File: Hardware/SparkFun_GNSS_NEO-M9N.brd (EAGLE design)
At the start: 64.9 x 38 mm, 74 parts, among them J1 MICROMOD_STANDARD, J4 Bus Selection, U1 U-BLOX_NEO-M9N, U2 3.3V, U3 EEPROM, U4 74HC1G04

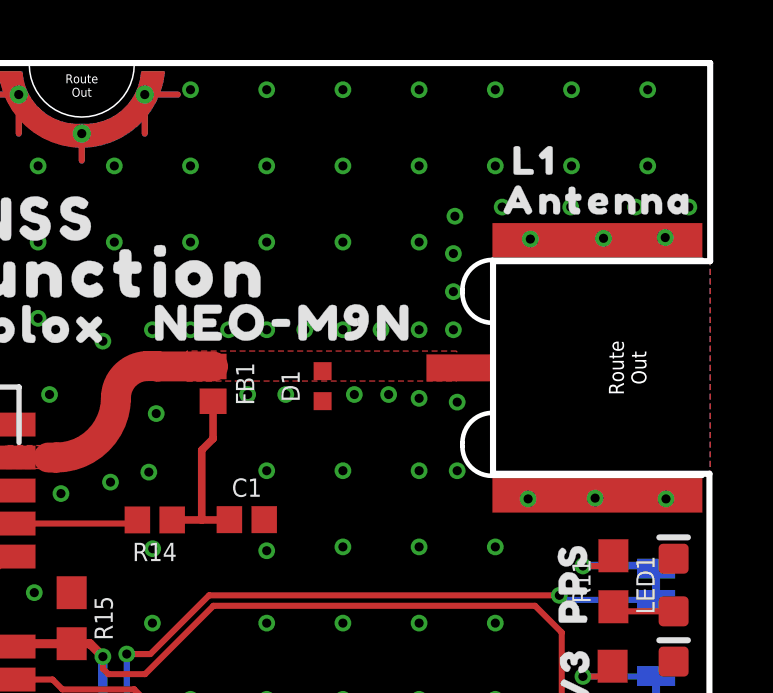
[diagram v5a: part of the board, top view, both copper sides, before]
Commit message: Switches SMA connector to PTH connector
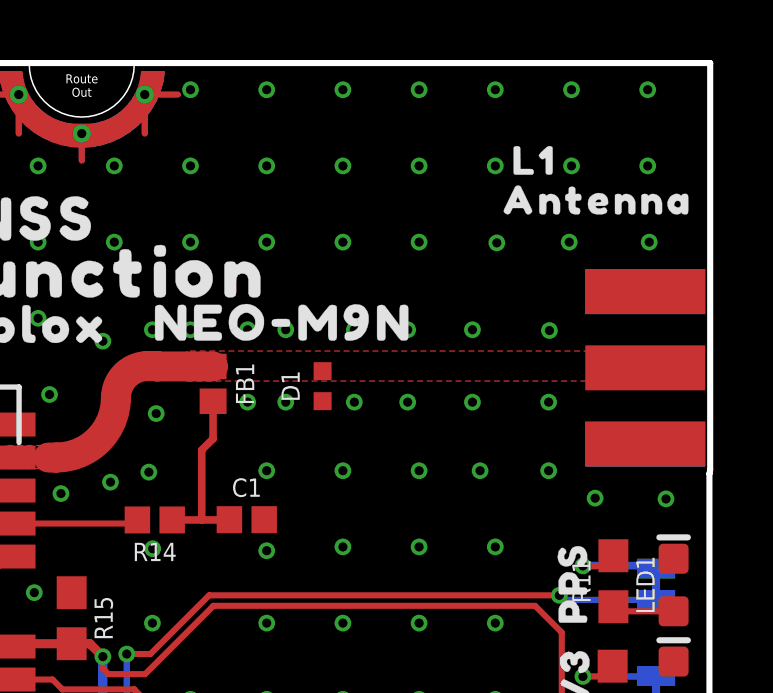
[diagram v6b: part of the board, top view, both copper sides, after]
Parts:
- E1: value ANTENNA-SMA-GROUNDEDEDGE_SMA_SMD -> ANTENNA-SMA-GROUNDEDEDGE_SMA; device SparkFun-RF:SMA-EDGE-SMD -> SparkFun-RF:SMA-EDGE
- moved E1 1.91 mm to (62.8, 27.9)
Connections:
- net GND: now also E1.GND@2, E1.GND@3
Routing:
- net GND: vias 209 -> 201
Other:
- outline, holes or cut-outs redrawn
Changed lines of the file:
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@@
 <layer number="19" name="Unrouted" color="6" fill="1" visible="yes" active="yes"/>
 <layer number="20" name="Dimension" color="15" fill="1" visible="yes" active="yes"/>
-<layer number="21" name="tPlace" color="16" fill="1" visible="yes" active="yes"/>
-<layer number="22" name="bPlace" color="14" fill="1" visible="yes" active="yes"/>
+<layer number="21" name="tPlace" color="16" fill="1" visible="no" active="yes"/>
+<layer number="22" name="bPlace" color="14" fill="1" visible="no" active="yes"/>
 <layer number="23" name="tOrigins" color="15" fill="1" visible="yes" active="yes"/>
 <layer number="24" name="bOrigins" color="15" fill="1" visible="yes" active="yes"/>
@@
 <layer number="37" name="tTest" color="7" fill="1" visible="no" active="yes"/>
 <layer number="38" name="bTest" color="7" fill="1" visible="no" active="yes"/>
-<layer number="39" name="tKeepout" color="4" fill="11" visible="no" active="yes"/>
+<layer number="39" name="tKeepout" color="4" fill="11" visible="yes" active="yes"/>
 <layer number="40" name="bKeepout" color="1" fill="11" visible="no" active="yes"/>
 <layer number="41" name="tRestrict" color="4" fill="10" visible="no" active="yes"/>
@@
 <layer number="115" name="ReferenceISLANDS" color="7" fill="1" visible="no" active="no"/>
 <layer number="116" name="Patch_BOT" color="9" fill="4" visible="no" active="no"/>
-<layer number="117" name="PM_Ref" color="26" fill="1" visible="yes" active="yes"/>
+<layer number="117" name="PM_Ref" color="26" fill="1" visible="no" active="yes"/>
 <layer number="118" name="Rect_Pads" color="7" fill="1" visible="no" active="no"/>
-<layer number="119" name="PF_Ref" color="31" fill="1" visible="yes" active="yes"/>
-<layer number="120" name="WFL_Ref" color="25" fill="1" visible="yes" active="yes"/>
+<layer number="119" name="PF_Ref" color="31" fill="1" visible="no" active="yes"/>
+<layer number="120" name="WFL_Ref" color="25" fill="1" visible="no" active="yes"/>
 <layer number="121" name="_tsilk" color="7" fill="1" visible="no" active="no"/>
 <layer number="122" name="_bsilk" color="7" fill="1" visible="no" active="no"/>
@@
 <wire x1="4" y1="8.65" x2="3.9746" y2="0.0508" width="0.2032" layer="20"/>
 <wire x1="3.9746" y1="0.0508" x2="64.9224" y2="0.0508" width="0.2032" layer="20"/>
-<wire x1="64.9478" y1="31.496" x2="57.7088" y2="31.496" width="0.2032" layer="20"/>
-<wire x1="57.7088" y1="31.496" x2="57.7088" y2="24.4094" width="0.2032" layer="20"/>
-<wire x1="57.7088" y1="24.4094" x2="64.9224" y2="24.4094" width="0.2032" layer="20"/>
-<wire x1="64.9478" y1="31.496" x2="64.9478" y2="38.1" width="0.2032" layer="20"/>
+<wire x1="64.9478" y1="38.1" x2="64.9478" y2="24.5364" width="0.2032" layer="20"/>
+<wire x1="64.9478" y1="24.5364" x2="64.9224" y2="24.4094" width="0.2032" layer="20"/>
 <wire x1="64.9224" y1="24.4094" x2="64.9224" y2="0.0508" width="0.2032" layer="20"/>
 <text x="88.5" y="40" size="1.778" layer="51" font="vector" ratio="15">0.8mm PCB
@@
 <attribute name="VALUE" x="62.5348" y="10.16" size="0.762" layer="27" rot="R90" align="center"/>
 </element>
-<element name="E1" library="SparkFun-RF" package="SMA-EDGE-SMD" value="ANTENNA-SMA-GROUNDEDEDGE_SMA_SMD" x="64.6884" y="27.94" smashed="yes" rot="R270">
-<attribute name="PROD_ID" value="CONN-15100" x="64.6884" y="27.94" size="1.778" layer="27" rot="R270" display="off"/>
+<element name="E1" library="SparkFun-RF" package="SMA-EDGE" value="ANTENNA-SMA-GROUNDEDEDGE_SMA" x="62.7834" y="27.94" smashed="yes" rot="R270">
+<attribute name="PROD_ID" value="CONN-08289" x="62.7834" y="27.94" size="1.778" layer="27" rot="R270" display="off"/>
 </element>
 <element name="FB1" library="SparkFun-Coils" package="0402" value="120Ω" x="48.3774" y="27.4064" smashed="yes" rot="R270">
@@
 <via x="34.417" y="15.113" extent="1-16" drill="0.3048"/>
 <via x="34.417" y="17.272" extent="1-16" drill="0.3048"/>
-<via x="56.4388" y="32.9946" extent="1-16" drill="0.3048"/>
-<via x="60.2996" y="33.2994" extent="1-16" drill="0.3048"/>
-<via x="62.4586" y="33.2994" extent="1-16" drill="0.3048"/>
-<via x="64.2366" y="33.2994" extent="1-16" drill="0.3048"/>
-<via x="56.388" y="29.21" extent="1-16" drill="0.3048"/>
+<via x="57.8358" y="32.1056" extent="1-16" drill="0.3048"/>
 <via x="42.926" y="27.051" extent="1-16" drill="0.3048"/>
 <via x="46.236" y="24.464" extent="1-16" drill="0.3048"/>
@@
 <wire x1="44" y1="35.75" x2="43.2" y2="35.75" width="0.2032" layer="1"/>
 <wire x1="43.2" y1="35.75" x2="41.9" y2="37.05" width="0.2032" layer="1"/>
-<via x="61.3918" y="32.258" extent="1-16" drill="0.3048"/>
-<via x="63.4492" y="32.2834" extent="1-16" drill="0.3048"/>
-<via x="58.9534" y="32.2326" extent="1-16" drill="0.3048"/>
-<via x="58.8772" y="23.5712" extent="1-16" drill="0.3048"/>
+<via x="60.2488" y="32.131" extent="1-16" drill="0.3048"/>
+<via x="59.5884" y="29.1846" extent="1-16" drill="0.3048"/>
 <via x="61.1124" y="23.5966" extent="1-16" drill="0.3048"/>
 <via x="63.4746" y="23.5712" extent="1-16" drill="0.3048"/>
@@
 <via x="34.3916" y="36.7284" extent="1-16" drill="0.3048"/>
 <via x="40.005" y="4.191" extent="1-16" drill="0.3048"/>
-<via x="58.0136" y="33.2994" extent="1-16" drill="0.3048"/>
 <contactref element="U$8" pad="7"/>
 <contactref element="U$15" pad="7"/>
@@
 <via x="52.705" y="24.511" extent="1-16" drill="0.3048"/>
 <via x="55.245" y="24.511" extent="1-16" drill="0.3048"/>
-<via x="55.245" y="29.21" extent="1-16" drill="0.3048"/>
-<via x="53.975" y="29.21" extent="1-16" drill="0.3048"/>
-<via x="52.705" y="29.21" extent="1-16" drill="0.3048"/>
+<via x="54.864" y="29.21" extent="1-16" drill="0.3048"/>
+<via x="53.086" y="29.21" extent="1-16" drill="0.3048"/>
 <via x="44.704" y="28.829" extent="1-16" drill="0.3048"/>
 <via x="46.482" y="26.416" extent="1-16" drill="0.3048"/>
 <via x="43.307" y="23.749" extent="1-16" drill="0.3048"/>
 <via x="44.958" y="24.13" extent="1-16" drill="0.3048"/>
-<via x="56.388" y="30.48" extent="1-16" drill="0.3048"/>
-<via x="56.388" y="31.75" extent="1-16" drill="0.3048"/>
-<via x="56.515" y="24.511" extent="1-16" drill="0.3048"/>
-<via x="56.515" y="26.797" extent="1-16" drill="0.3048"/>
-<via x="55.245" y="26.924" extent="1-16" drill="0.3048"/>
-<via x="54.229" y="27.051" extent="1-16" drill="0.3048"/>
-<via x="53.086" y="27.051" extent="1-16" drill="0.3048"/>
-<via x="51.435" y="29.21" extent="1-16" drill="0.3048"/>
-<via x="50.8" y="27.051" extent="1-16" drill="0.3048"/>
-<via x="49.53" y="27.051" extent="1-16" drill="0.3048"/>
-<via x="50.165" y="29.21" extent="1-16" drill="0.3048"/>
-<via x="48.895" y="29.21" extent="1-16" drill="0.3048"/>
+<via x="57.023" y="29.21" extent="1-16" drill="0.3048"/>
+<via x="57.277" y="24.511" extent="1-16" drill="0.3048"/>
+<via x="59.563" y="26.797" extent="1-16" drill="0.3048"/>
+<via x="57.023" y="26.797" extent="1-16" drill="0.3048"/>
+<via x="54.864" y="26.797" extent="1-16" drill="0.3048"/>
+<via x="53.086" y="26.797" extent="1-16" drill="0.3048"/>
+<via x="50.8" y="29.21" extent="1-16" drill="0.3048"/>
+<via x="50.8" y="26.797" extent="1-16" drill="0.3048"/>
+<via x="49.53" y="26.797" extent="1-16" drill="0.3048"/>
+<via x="49.53" y="29.21" extent="1-16" drill="0.3048"/>
 <via x="47.625" y="29.21" extent="1-16" drill="0.3048"/>
 <via x="46.355" y="29.21" extent="1-16" drill="0.3048"/>
@@
 <via x="21.8186" y="24.4856" extent="1-16" drill="0.3048"/>
 <via x="18.1864" y="27.3812" extent="1-16" drill="0.3048"/>
+<contactref element="E1" pad="GND@2"/>
+<contactref element="E1" pad="GND@3"/>
+<via x="62.9158" y="32.131" extent="1-16" drill="0.3048"/>
+<via x="59.563" y="24.511" extent="1-16" drill="0.3048"/>
 </signal>
 <signal name="SCL/SCK">
@@
 <vertex x="47.5" y="28.5"/>
 <vertex x="47.5" y="27.5"/>
-<vertex x="56.5" y="27.5"/>
-<vertex x="56.5" y="28.5"/>
+<vertex x="62.85" y="27.5"/>
+<vertex x="62.85" y="28.5"/>
 </polygon>
 <wire x1="48.3774" y1="27.9864" x2="46.5136" y2="27.9864" width="1" layer="1"/>

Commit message: Adds PTH SMA Connector to design
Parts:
- E1: value ANTENNA-SMA-GROUNDEDEDGE_SMA -> ANTENNA-SMA-GROUNDEDEDGE_SMA_THIN
- moved FRAME2 26.9 mm to (-2.54, -12.7)
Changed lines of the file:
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@@
 <layer number="19" name="Unrouted" color="6" fill="1" visible="yes" active="yes"/>
 <layer number="20" name="Dimension" color="15" fill="1" visible="yes" active="yes"/>
-<layer number="21" name="tPlace" color="16" fill="1" visible="no" active="yes"/>
-<layer number="22" name="bPlace" color="14" fill="1" visible="no" active="yes"/>
+<layer number="21" name="tPlace" color="16" fill="1" visible="yes" active="yes"/>
+<layer number="22" name="bPlace" color="14" fill="1" visible="yes" active="yes"/>
 <layer number="23" name="tOrigins" color="15" fill="1" visible="yes" active="yes"/>
 <layer number="24" name="bOrigins" color="15" fill="1" visible="yes" active="yes"/>
@@
 <layer number="37" name="tTest" color="7" fill="1" visible="no" active="yes"/>
 <layer number="38" name="bTest" color="7" fill="1" visible="no" active="yes"/>
-<layer number="39" name="tKeepout" color="4" fill="11" visible="yes" active="yes"/>
+<layer number="39" name="tKeepout" color="4" fill="11" visible="no" active="yes"/>
 <layer number="40" name="bKeepout" color="1" fill="11" visible="no" active="yes"/>
 <layer number="41" name="tRestrict" color="4" fill="10" visible="no" active="yes"/>
@@
 <board>
 <plain>
-<text x="33.02" y="-24.511" size="1.778" layer="51" font="vector">Elias Santistevan</text>
+<text x="29.21" y="-13.081" size="1.778" layer="51" font="vector">Elias Santistevan</text>
 <wire x1="0" y1="9.125" x2="0" y2="15.825" width="0.2032" layer="20"/>
 <wire x1="0" y1="17.025" x2="0" y2="28.975" width="0.2032" layer="20"/>
@@
 <attribute name="VALUE" x="62.5348" y="10.16" size="0.762" layer="27" rot="R90" align="center"/>
 </element>
-<element name="E1" library="SparkFun-RF" package="SMA-EDGE" value="ANTENNA-SMA-GROUNDEDEDGE_SMA" x="62.7834" y="27.94" smashed="yes" rot="R270">
-<attribute name="PROD_ID" value="CONN-08289" x="62.7834" y="27.94" size="1.778" layer="27" rot="R270" display="off"/>
+<element name="E1" library="SparkFun-RF" package="SMA-EDGE" value="ANTENNA-SMA-GROUNDEDEDGE_SMA_THIN" x="62.7834" y="27.94" smashed="yes" rot="R270">
+<attribute name="PROD_ID" value="CONN-16309" x="62.7834" y="27.94" size="1.778" layer="27" rot="R270" display="off"/>
 </element>
 <element name="FB1" library="SparkFun-Coils" package="0402" value="120Ω" x="48.3774" y="27.4064" smashed="yes" rot="R270">
@@
 <attribute name="VALUE" x="9.706" y="4.699" size="0.6096" layer="27" font="vector" ratio="20" rot="R90" align="top-center"/>
 </element>
-<element name="FRAME2" library="SparkFun-Aesthetics" package="CREATIVE_COMMONS" value="FRAME-LEDGER" x="1.27" y="-39.37" smashed="yes">
-<attribute name="DESIGNER" value="" x="1.27" y="-39.37" size="1.778" layer="27" font="vector" ratio="15" display="off"/>
-<attribute name="REV" value="" x="1.27" y="-39.37" size="1.778" layer="27" font="vector" ratio="15" display="off"/>
+<element name="FRAME2" library="SparkFun-Aesthetics" package="CREATIVE_COMMONS" value="FRAME-LEDGER" x="-2.54" y="-12.7" smashed="yes">
+<attribute name="DESIGNER" value="" x="-2.54" y="-12.7" size="1.778" layer="27" font="vector" ratio="15" display="off"/>
+<attribute name="REV" value="" x="-2.54" y="-12.7" size="1.778" layer="27" font="vector" ratio="15" display="off"/>
 </element>
 <element name="U$18" library="top" package="#BUS_SELECT#509" value="" x="24.892" y="37.084" smashed="yes"/>

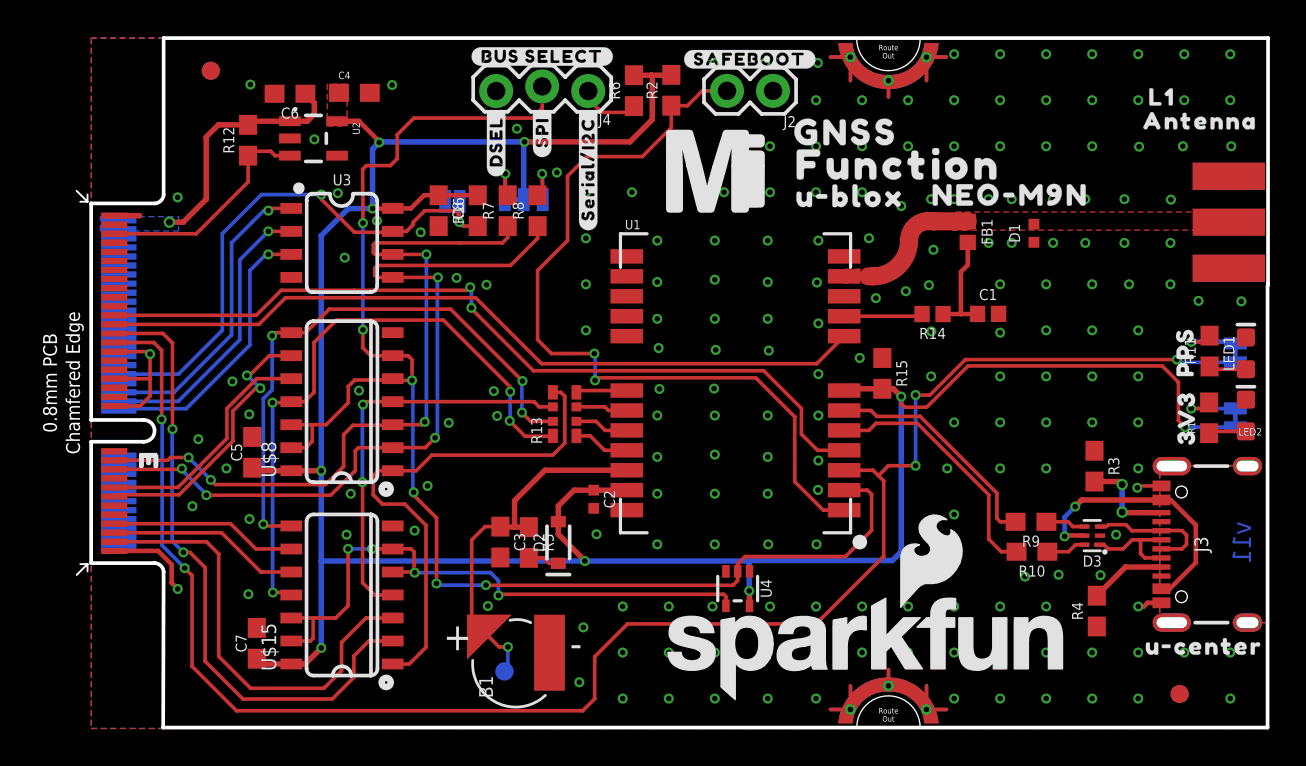
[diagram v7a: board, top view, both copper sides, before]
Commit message: Adds a via, moves "L1" text
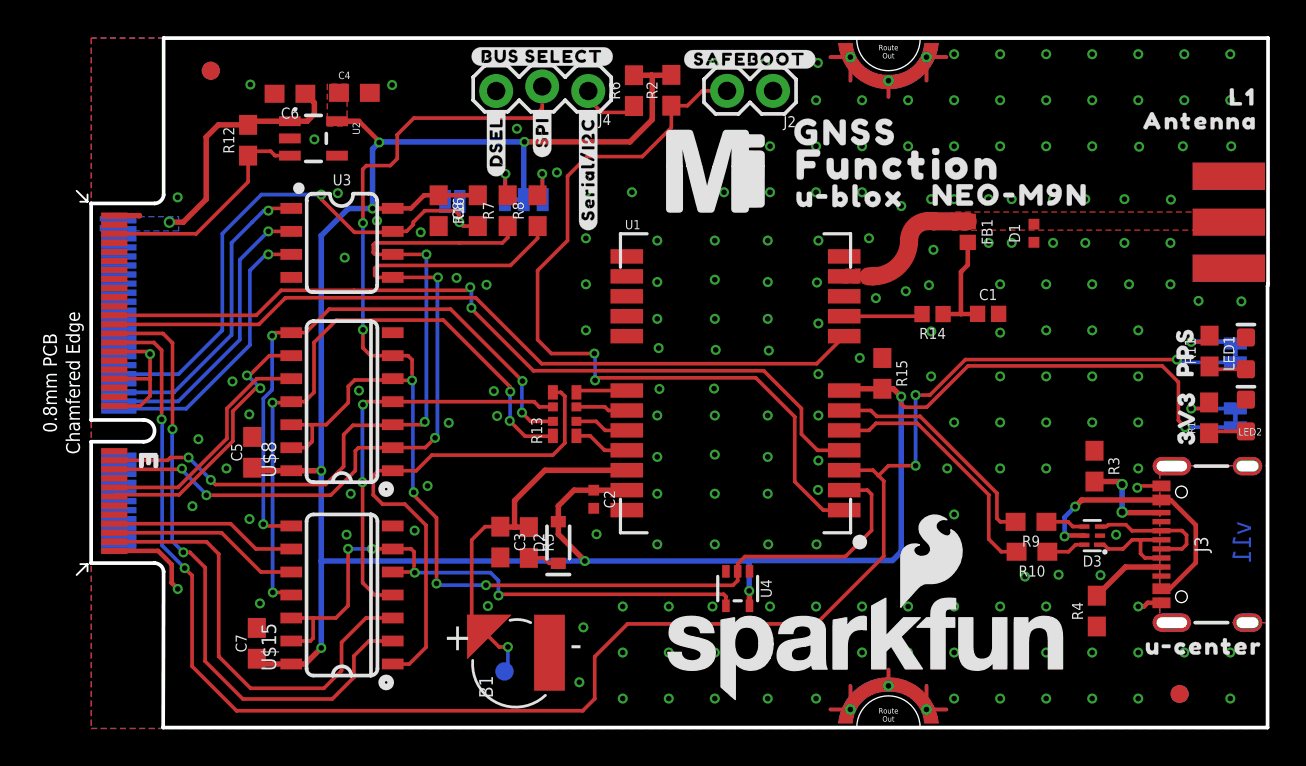
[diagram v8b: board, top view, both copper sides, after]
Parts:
- moved U$14 4.45 mm to (63.6, 34.8)
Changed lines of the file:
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@@
 <layer number="115" name="ReferenceISLANDS" color="7" fill="1" visible="no" active="no"/>
 <layer number="116" name="Patch_BOT" color="9" fill="4" visible="no" active="no"/>
-<layer number="117" name="PM_Ref" color="26" fill="1" visible="no" active="yes"/>
+<layer number="117" name="PM_Ref" color="26" fill="1" visible="yes" active="yes"/>
 <layer number="118" name="Rect_Pads" color="7" fill="1" visible="no" active="no"/>
-<layer number="119" name="PF_Ref" color="31" fill="1" visible="no" active="yes"/>
-<layer number="120" name="WFL_Ref" color="25" fill="1" visible="no" active="yes"/>
+<layer number="119" name="PF_Ref" color="31" fill="1" visible="yes" active="yes"/>
+<layer number="120" name="WFL_Ref" color="25" fill="1" visible="yes" active="yes"/>
 <layer number="121" name="_tsilk" color="7" fill="1" visible="no" active="no"/>
 <layer number="122" name="_bsilk" color="7" fill="1" visible="no" active="no"/>
@@
 <element name="U$11" library="SparkFun-MicroMod" package="MICROMOD_MI_LOGO_1" value="" x="34.4932" y="30.7848" smashed="yes"/>
 <element name="U$4" library="top" package="#SAFEBOOT#12" value="" x="36.3474" y="36.9316" smashed="yes"/>
-<element name="U$14" library="top" package="L1321542" value="" x="59.1058" y="34.8488" smashed="yes"/>
+<element name="U$14" library="top" package="L1321542" value="" x="63.5508" y="34.8488" smashed="yes"/>
 <element name="U$8" library="SparkFun-IC-Logic" package="SO14" value="74LVC4066D_QUAD_BILATERAL_SWITCH" x="13.843" y="17.399" smashed="yes" rot="R90">
 <attribute name="NAME" x="10.2108" y="13.843" size="0.8128" layer="25" font="vector" ratio="16" rot="R90"/>
@@
 <contactref element="C7" pad="2"/>
 <via x="8.727" y="17.3344" extent="1-16" drill="0.3048"/>
-<via x="8.679" y="7.4094" extent="1-16" drill="0.3048"/>
+<via x="9.314" y="6.9014" extent="1-16" drill="0.3048"/>
 <via x="37.398" y="20.852" extent="1-16" drill="0.3048"/>
 <via x="34.468" y="20.892" extent="1-16" drill="0.3048"/>
